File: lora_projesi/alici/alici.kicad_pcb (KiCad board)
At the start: 4 copper layers, 88 x 102 mm, 127 parts, among them J1 USB-C, J2 SMA, J3 RJ45, J4 u.FL (ANA ANTEN), J5 12 V GIRIS, J6 LAMBA, J7 MICRO-SIM, J8 u.FL (YARDIMCI ANTEN, ISTEGE 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, K1 SRD-12VDC-SL-A, Q1 AO3401A, Q2 MMBT2222A, Q3 MMBT2222A, Q4 MMBT2222A, SW1 DUGME, U1 ESP32-S3-WROOM-1-N4, U10 SIM7600SA, U11 AP2112K-3.3, U12 ESDA6V1-5SC6, U4 RFM95W-915S2, U5 TPS62933DRLR, U6 TPS62933DRLR, U7 USBLC6-2SC6, U8 TXB0104PW, U9 W5500, Y1 25 MHz

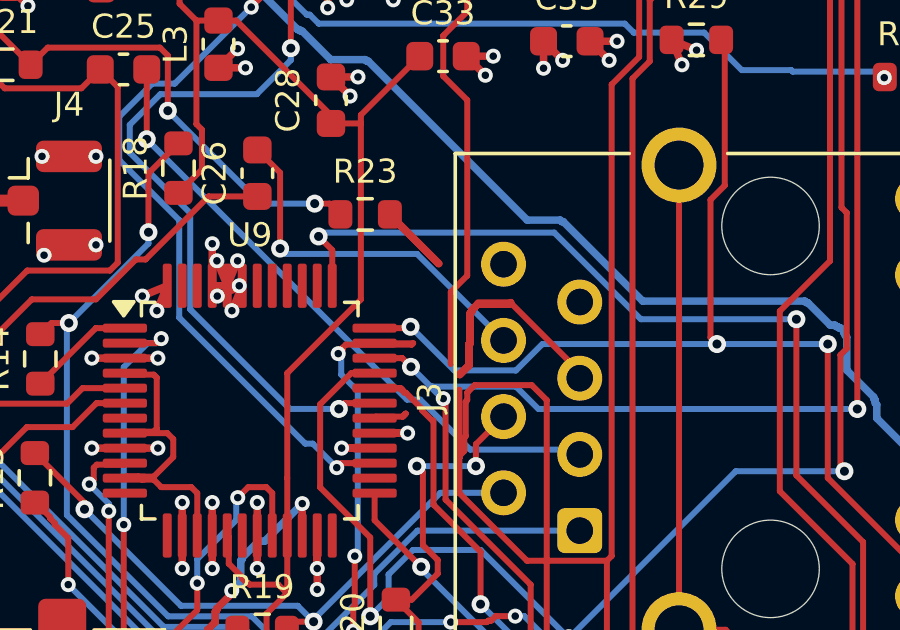
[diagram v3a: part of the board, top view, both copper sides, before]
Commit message: izgara: uc noktalarini yakala, bosluk payi
Co-Authored-By: Claude Sonnet 5.5 <noreply@anthropic.com>
Claude-Session: https://claude.ai/code/session_01Q71gHQtKJ86ZE2CtYTYSwP
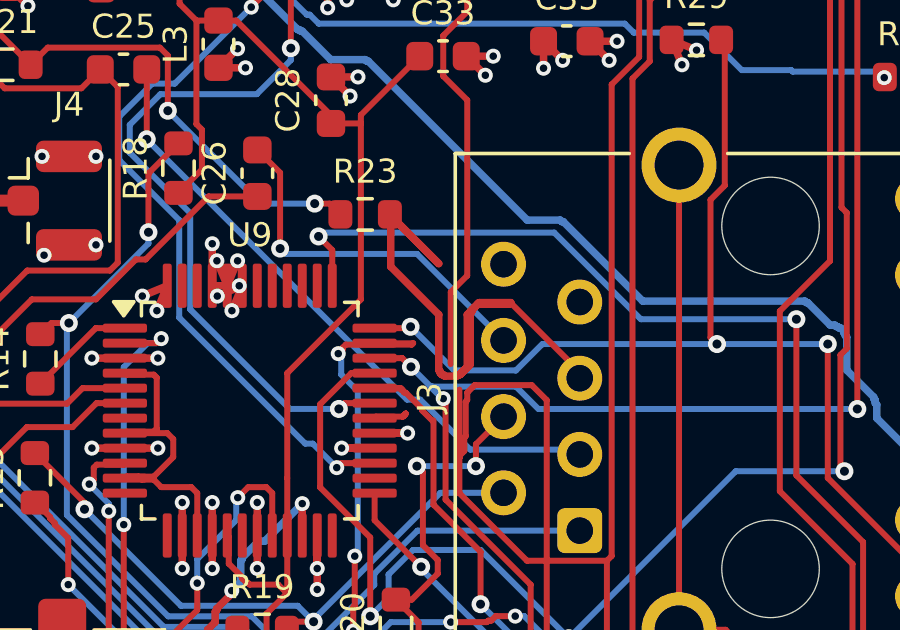
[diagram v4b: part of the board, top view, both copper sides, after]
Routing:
- net RCT: track 16.7 -> 32.4 mm
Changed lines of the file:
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@@
   (segment (start 61.75 62) (end 62.1 62.35) (width 0.2) (layer "F.Cu") (net 20))
   (segment (start 60.1625 61.25) (end 61.0447 61.25) (width 0.2) (layer "F.Cu") (net 20))
+  (segment (start 61.15 61.4) (end 61.2 61.4) (width 0.2) (layer "F.Cu") (net 20))
   (segment (start 62.1241 62.3294) (end 62.1241 65.1352) (width 0.2) (layer "F.Cu") (net 20))
-  (segment (start 61.2 61.4) (end 61.75 61.95) (width 0.2) (layer "F.Cu") (net 20))
-  (segment (start 61.15 61.4) (end 61.2 61.4) (width 0.2) (layer "F.Cu") (net 20))
   (segment (start 61.05 61.3) (end 61.1 61.3) (width 0.2) (layer "F.Cu") (net 20))
   (segment (start 62.1241 65.1352) (end 63.6935 66.7046) (width 0.2) (layer "F.Cu") (net 20))
+  (segment (start 61.2 61.4) (end 61.75 61.95) (width 0.2) (layer "F.Cu") (net 20))
   (via (at 63.6935 68.4525) (size 0.6) (drill 0.3) (layers "F.Cu" "B.Cu") (net 20))
   (via (at 71.6417 70.6825) (size 0.6) (drill 0.3) (layers "F.Cu" "B.Cu") (net 20))
@@
   (segment (start 63.35 59.75) (end 63.35 58.75) (width 0.25) (layer "F.Cu") (net 56))
   (segment (start 67 60.7082) (end 64.6818 58.39) (width 0.2) (layer "F.Cu") (net 56))
+  (segment (start 63.25 60.55) (end 63 60.8) (width 0.25) (layer "F.Cu") (net 56))
   (segment (start 63.35 58.75) (end 63.4 58.7) (width 0.25) (layer "F.Cu") (net 56))
+  (segment (start 62.3 58.8) (end 60.7 57.2) (width 0.25) (layer "F.Cu") (net 56))
   (segment (start 63.6 58.45) (end 64.65 58.45) (width 0.25) (layer "F.Cu") (net 56))
   (segment (start 63.4 58.65) (end 63.6 58.45) (width 0.25) (layer "F.Cu") (net 56))
+  (segment (start 60.7 55.5) (end 60.65 55.45) (width 0.25) (layer "F.Cu") (net 56))
+  (segment (start 63.35 60.45) (end 63 60.8) (width 0.25) (layer "F.Cu") (net 56))
+  (segment (start 62.95 60.8) (end 62.9 60.85) (width 0.25) (layer "F.Cu") (net 56))
   (segment (start 60.65 55.45) (end 62.3 57.1) (width 0.25) (layer "F.Cu") (net 56))
   (segment (start 63.4 58.7) (end 63.4 58.65) (width 0.25) (layer "F.Cu") (net 56))
   (segment (start 63.3 59.8) (end 63.35 59.75) (width 0.25) (layer "F.Cu") (net 56))
+  (segment (start 62.45 60.8) (end 62.4 60.8) (width 0.25) (layer "F.Cu") (net 56))
+  (segment (start 63.65 58.4) (end 63.25 58.8) (width 0.25) (layer "F.Cu") (net 56))
   (segment (start 63 60.8) (end 63.3 60.5) (width 0.25) (layer "F.Cu") (net 56))
   (segment (start 63.6 58.45) (end 64.65 58.45) (width 0.25) (layer "F.Cu") (net 56))
+  (segment (start 63 60.8) (end 62.95 60.8) (width 0.25) (layer "F.Cu") (net 56))
   (segment (start 63.3 59.8) (end 63.35 59.75) (width 0.25) (layer "F.Cu") (net 56))
+  (segment (start 62.5 60.85) (end 62.45 60.8) (width 0.25) (layer "F.Cu") (net 56))
   (segment (start 63.35 59.75) (end 63.35 58.75) (width 0.25) (layer "F.Cu") (net 56))
   (segment (start 60.65 55.45) (end 62.3 57.1) (width 0.25) (layer "F.Cu") (net 56))
   (segment (start 67 60.92) (end 67 60.7082) (width 0.2) (layer "F.Cu") (net 56))
+  (segment (start 63.35 58.7) (end 63.35 60.45) (width 0.25) (layer "F.Cu") (net 56))
   (segment (start 63.3 60.5) (end 63.3 59.8) (width 0.25) (layer "F.Cu") (net 56))
   (segment (start 64.65 58.45) (end 64.7 58.4) (width 0.25) (layer "F.Cu") (net 56))
+  (segment (start 62.35 60.7) (end 62.3 60.65) (width 0.25) (layer "F.Cu") (net 56))
+  (segment (start 60.7 57.2) (end 60.7 55.5) (width 0.25) (layer "F.Cu") (net 56))
+  (segment (start 62.3 60.65) (end 62.3 58.8) (width 0.25) (layer "F.Cu") (net 56))
+  (segment (start 63.65 58.4) (end 63.35 58.7) (width 0.25) (layer "F.Cu") (net 56))
   (segment (start 63 60.8) (end 63.3 60.5) (width 0.25) (layer "F.Cu") (net 56))
+  (segment (start 64.7 58.4) (end 63.65 58.4) (width 0.25) (layer "F.Cu") (net 56))
+  (segment (start 63.25 58.8) (end 63.25 60.55) (width 0.25) (layer "F.Cu") (net 56))
+  (segment (start 62.9 60.85) (end 62.5 60.85) (width 0.25) (layer "F.Cu") (net 56))
+  (segment (start 63.65 58.4) (end 63.35 58.7) (width 0.25) (layer "F.Cu") (net 56))
+  (segment (start 62.4 60.8) (end 62.35 60.75) (width 0.25) (layer "F.Cu") (net 56))
   (segment (start 64.6818 58.39) (end 63.6025 58.39) (width 0.2) (layer "F.Cu") (net 56))
+  (segment (start 62.35 60.75) (end 62.35 60.7) (width 0.25) (layer "F.Cu") (net 56))
   (segment (start 63.3 60.5) (end 63.3 59.8) (width 0.25) (layer "F.Cu") (net 56))
+  (segment (start 63.35 60.45) (end 63 60.8) (width 0.25) (layer "F.Cu") (net 56))
+  (segment (start 63.35 58.7) (end 63.35 60.45) (width 0.25) (layer "F.Cu") (net 56))
   (segment (start 57.0121 56.5976) (end 57.0121 54.0691) (width 0.2) (layer "F.Cu") (net 57))
   (segment (start 57.0121 54.0691) (end 56.2539 53.3109) (width 0.2) (layer "F.Cu") (net 57))
@@
   (segment (start 62.2888 45.1841) (end 59.8426 45.1841) (width 0.2) (layer "F.Cu") (net 91))
   (segment (start 62.7 60.45) (end 62.7 58.05) (width 0.2) (layer "F.Cu") (net 91))
+  (segment (start 61.1 62.2) (end 61.2 62.1) (width 0.2) (layer "F.Cu") (net 91))
   (segment (start 62.45 50.85) (end 62.45 49.5) (width 0.2) (layer "F.Cu") (net 91))
   (segment (start 62.45 49.5) (end 63.25 48.7) (width 0.2) (layer "F.Cu") (net 91))
@@
   (segment (start 62.7 58.05) (end 63.25 57.5) (width 0.2) (layer "F.Cu") (net 91))
   (segment (start 63.25 57.5) (end 63.25 51.65) (width 0.2) (layer "F.Cu") (net 91))
+  (segment (start 61.1 62.2) (end 61.2 62.1) (width 0.2) (layer "F.Cu") (net 91))
   (segment (start 57.3696 49.9189) (end 57.3696 46.0071) (width 0.2) (layer "F.Cu") (net 92))
   (segment (start 59.8426 43.4584) (end 62.1083 41.1927) (width 0.2) (layer "F.Cu") (net 92))

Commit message: Alici: ara hal (+3V3A, XI, ETH_CS agi yeniden cizdiriliyor)
Co-Authored-By: Claude Sonnet 5.5 <noreply@anthropic.com>
Claude-Session: https://claude.ai/code/session_01Q71gHQtKJ86ZE2CtYTYSwP
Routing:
- net +3V3A: track 80.8 -> 0.00 mm
- net XO: track 42.9 -> 0.00 mm, vias 2 -> 0
- net XI: track 23.9 -> 0.00 mm
- net ETH_CS: track 21.7 -> 0.00 mm, vias 2 -> 0
- net RCT: track 32.4 -> 40.3 mm, vias 0 -> 2
- net LORA_DIO1: track 79.5 -> 82.1 mm

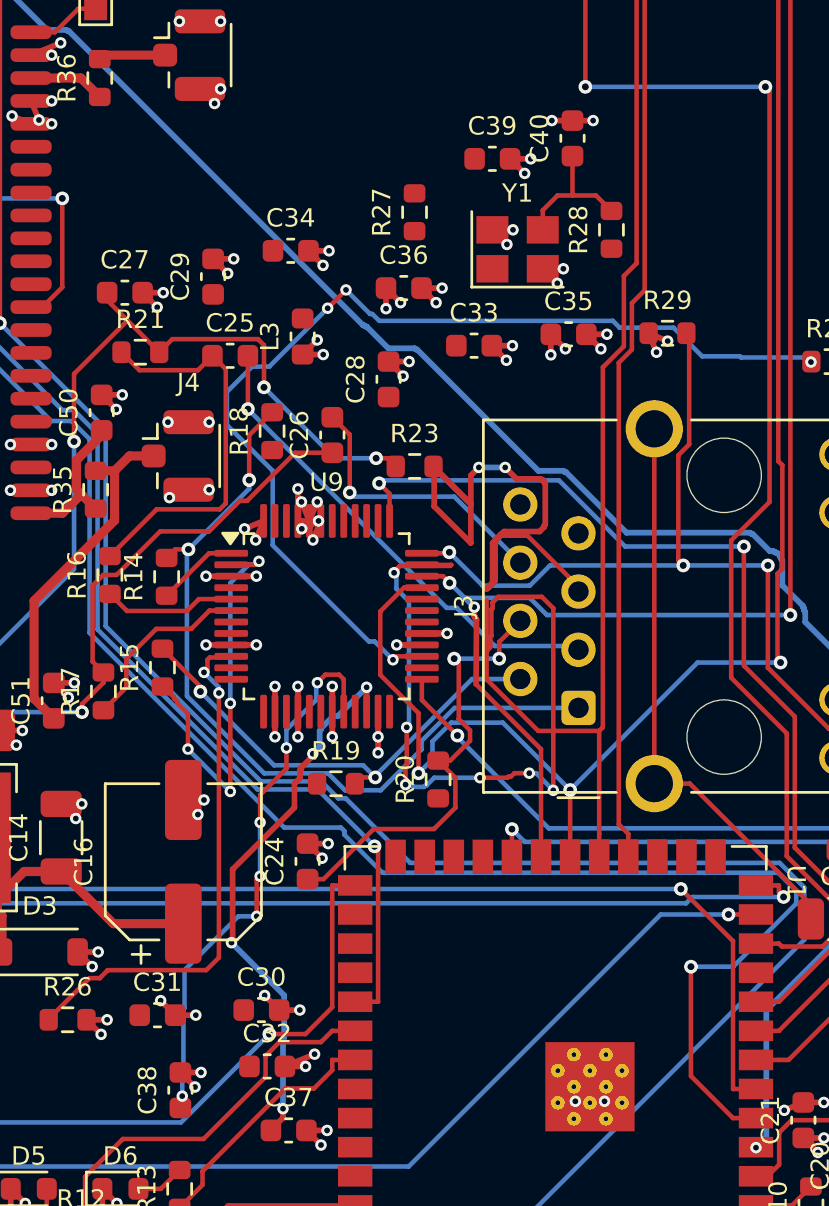
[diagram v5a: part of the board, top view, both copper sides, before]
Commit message: Alici: ETH dekuplaj kondansatorleri arka yuze (boru hatti suruyor)
Co-Authored-By: Claude Sonnet 5.5 <noreply@anthropic.com>
Claude-Session: https://claude.ai/code/session_01Q71gHQtKJ86ZE2CtYTYSwP
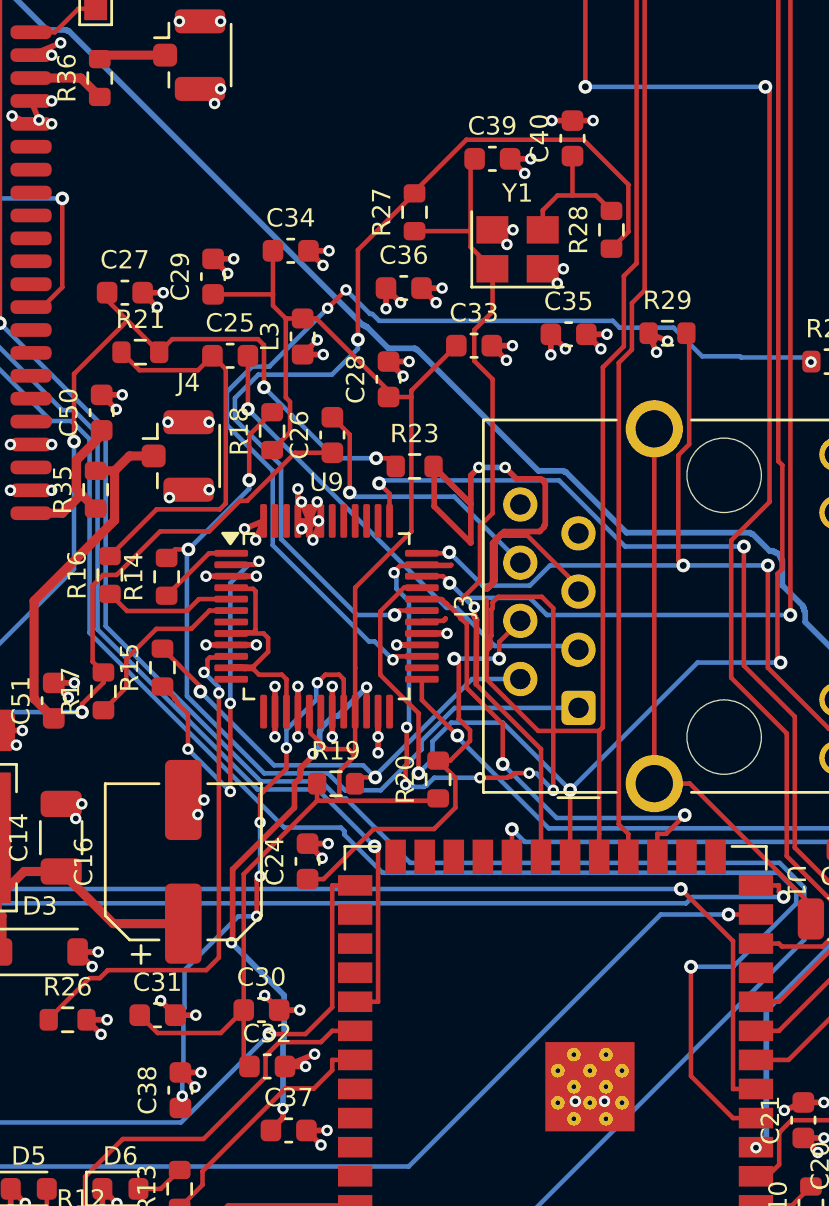
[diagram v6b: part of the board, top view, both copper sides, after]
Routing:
- net +3V3A: track 0.00 -> 80.8 mm
- net XO: track 0.00 -> 42.9 mm, vias 0 -> 2
- net XI: track 0.00 -> 25.1 mm
- net ETH_CS: track 0.00 -> 21.8 mm, vias 0 -> 2
